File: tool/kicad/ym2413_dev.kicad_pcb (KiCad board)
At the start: 2 copper layers, 34 parts, among them P1 CONN_4, U1 YM2413, X1 CRYSTAL

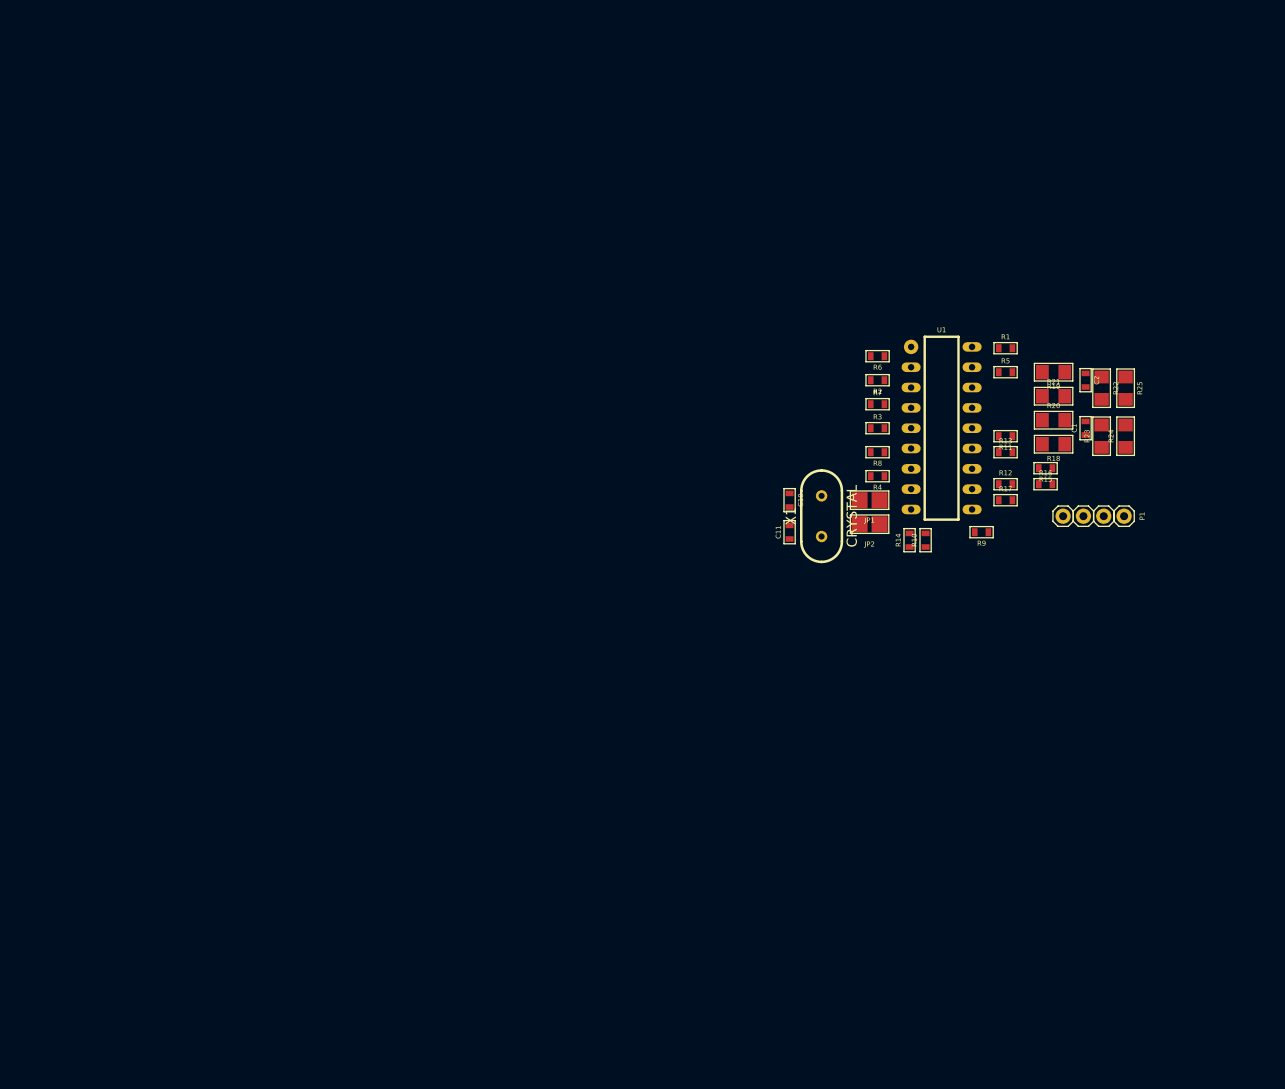
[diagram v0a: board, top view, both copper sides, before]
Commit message: cleanup; assign pins; add test points; restart pcb layout from zero
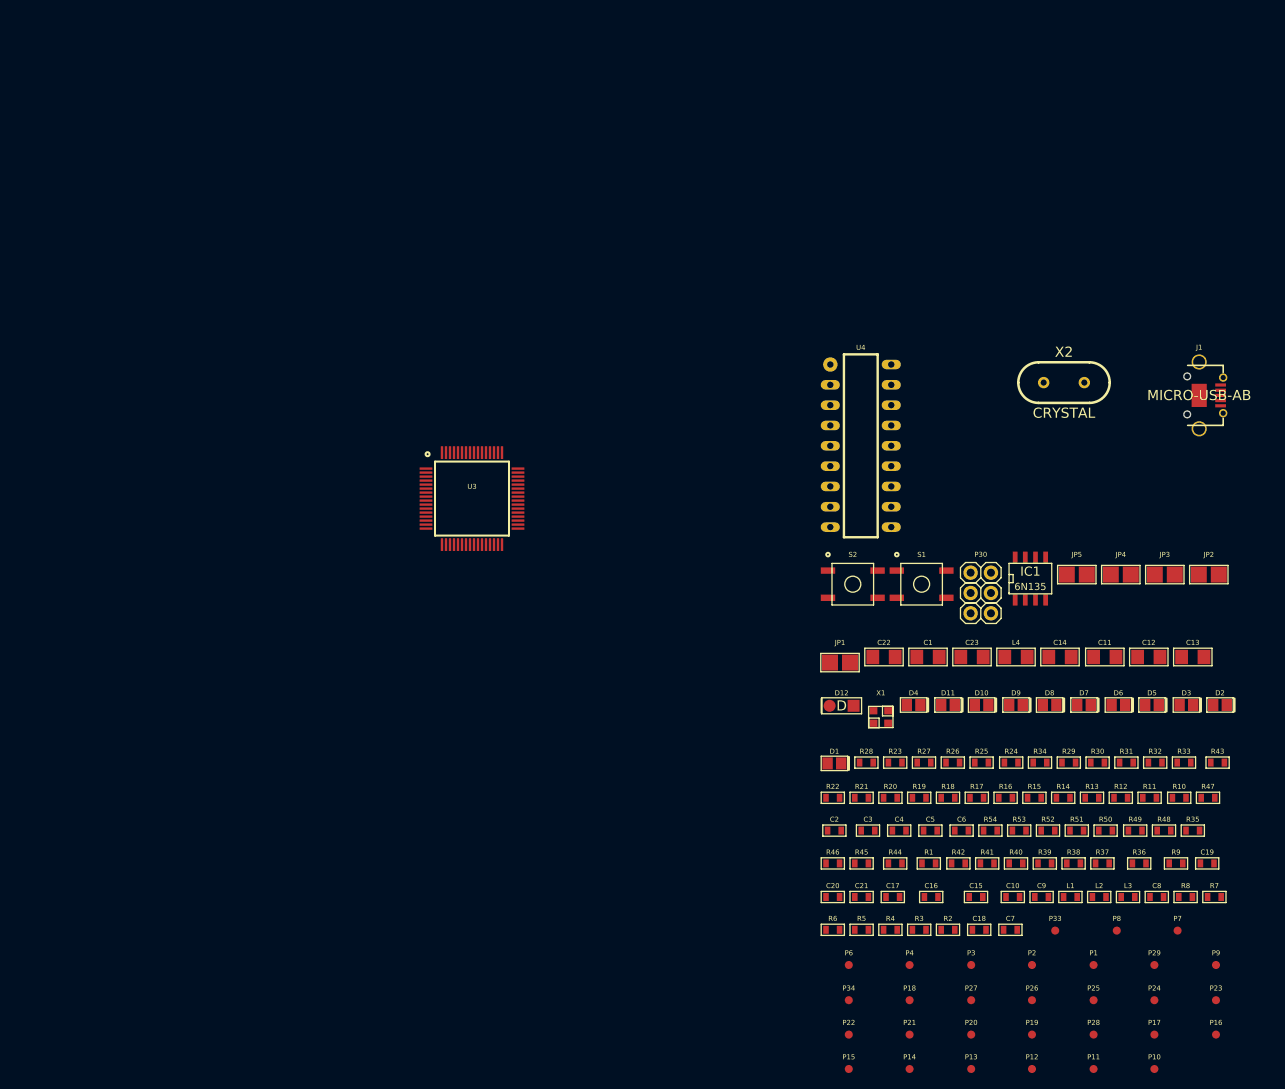
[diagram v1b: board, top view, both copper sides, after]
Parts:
- removed U1: YM2413, DIL18
- added C12: 4.7uF, 1206, F.Cu at (172.9, 126.6)
- added C13: 10uF, 1206, F.Cu at (178.4, 126.6)
- added C14: 10uF, 1206, F.Cu at (161.8, 126.6)
- added C15: 20pF/NC, 0603_S, F.Cu at (151.3, 156.6)
- added C16: 20pF/NC, 0603_S, F.Cu at (145.7, 156.6)
- added C17: 100nF, 0603_S, F.Cu at (140.9, 156.6)
- added C18: 2.2nF, 0603_S, F.Cu at (151.7, 160.7)
- added C19: 2.2nF, 0603_S, F.Cu at (180.2, 152.4)
- added C20: 1uF, 0603_S, F.Cu at (133.4, 156.6)
- added C21: 1uF, 0603_S, F.Cu at (137.0, 156.6)
- added C22: 10uF, 1206, F.Cu at (139.8, 126.6)
- added C23: 10uF, 1206, F.Cu at (150.8, 126.6)
- added C3: 100nF, 0603_S, F.Cu at (137.8, 148.3)
- added C4: 18pF, 0603_S, F.Cu at (141.7, 148.3)
- added C5: 100nF, 0603_S, F.Cu at (145.6, 148.3)
- added C6: 18pF, 0603_S, F.Cu at (149.5, 148.3)
- added C7: 1uF, 0603_S, F.Cu at (155.6, 160.7)
- added C8: 10nF, 0603_S, F.Cu at (173.9, 156.6)
- added C9: 1uF, 0603_S, F.Cu at (159.5, 156.6)
- added D1: LED, 0805_LED, F.Cu at (133.6, 139.9)
- added D10: LED, 0805_LED, F.Cu at (152.0, 132.6)
- added D11: LED, 0805_LED, F.Cu at (147.8, 132.6)
- added D12: D, TAIW_SEM_DIODE, F.Cu at (134.5, 132.7)
- added D2: LED, 0805_LED, F.Cu at (181.8, 132.6)
- added D3: LED, 0805_LED, F.Cu at (177.6, 132.6)
- added D4: LED, 0805_LED, F.Cu at (143.5, 132.6)
- added D5: LED, 0805_LED, F.Cu at (173.3, 132.6)
- added D6: LED, 0805_LED, F.Cu at (169.1, 132.6)
- added D7: LED, 0805_LED, F.Cu at (164.8, 132.6)
- added D8: LED, 0805_LED, F.Cu at (160.5, 132.6)
- added D9: LED, 0805_LED, F.Cu at (156.3, 132.6)
- added IC1: 6N135, SO8E, F.Cu at (158.1, 116.8)
- added J1: MICRO-USB-AB, USB-MICRO-AB-Molex-47590-0001, F.Cu at (179.2, 93.9)
- added JP3: SJ, Solder_Jumper_2mm, F.Cu at (174.9, 116.3)
- added JP4: SJ, Solder_Jumper_2mm, F.Cu at (169.4, 116.3)
- added JP5: SJ, Solder_Jumper_2mm, F.Cu at (163.9, 116.3)
- added L1: FB, 0603_S, F.Cu at (163.1, 156.6)
- added L2: FB, 0603_S, F.Cu at (166.7, 156.6)
- added L3: FB, 0603_S, F.Cu at (170.3, 156.6)
- added L4: L, 1206, F.Cu at (156.3, 126.6)
- added P10: TEST_POINT, Test_Pad_1mm, F.Cu at (173.6, 178.1)
- added P11: TEST_POINT, Test_Pad_1mm, F.Cu at (166.0, 178.1)
- added P12: TEST_POINT, Test_Pad_1mm, F.Cu at (158.3, 178.1)
- added P13: TEST_POINT, Test_Pad_1mm, F.Cu at (150.7, 178.1)
- added P14: TEST_POINT, Test_Pad_1mm, F.Cu at (143.0, 178.1)
- added P15: TEST_POINT, Test_Pad_1mm, F.Cu at (135.4, 178.1)
- added P16: TEST_POINT, Test_Pad_1mm, F.Cu at (181.3, 173.8)
- added P17: TEST_POINT, Test_Pad_1mm, F.Cu at (173.6, 173.8)
- added P18: TEST_POINT, Test_Pad_1mm, F.Cu at (143.0, 169.5)
- added P19: TEST_POINT, Test_Pad_1mm, F.Cu at (158.3, 173.8)
- added P2: TEST_POINT, Test_Pad_1mm, F.Cu at (158.3, 165.1)
- added P20: TEST_POINT, Test_Pad_1mm, F.Cu at (150.7, 173.8)
- added P21: TEST_POINT, Test_Pad_1mm, F.Cu at (143.0, 173.8)
- added P22: TEST_POINT, Test_Pad_1mm, F.Cu at (135.4, 173.8)
- added P23: TEST_POINT, Test_Pad_1mm, F.Cu at (181.3, 169.5)
- added P24: TEST_POINT, Test_Pad_1mm, F.Cu at (173.6, 169.5)
- added P25: TEST_POINT, Test_Pad_1mm, F.Cu at (166.0, 169.5)
- added P26: TEST_POINT, Test_Pad_1mm, F.Cu at (158.3, 169.5)
- added P27: TEST_POINT, Test_Pad_1mm, F.Cu at (150.7, 169.5)
- added P28: TEST_POINT, Test_Pad_1mm, F.Cu at (166.0, 173.8)
- added P29: TEST_POINT, Test_Pad_1mm, F.Cu at (173.6, 165.1)
- added P3: TEST_POINT, Test_Pad_1mm, F.Cu at (150.7, 165.1)
- added P30: CONN_3X2, PIN_2X3_ALT_S, F.Cu at (151.9, 118.6)
- added P33: TEST_POINT, Test_Pad_1mm, F.Cu at (161.2, 160.8)
- added P34: TEST_POINT, Test_Pad_1mm, F.Cu at (135.4, 169.5)
- added P4: TEST_POINT, Test_Pad_1mm, F.Cu at (143.0, 165.1)
- added P6: TEST_POINT, Test_Pad_1mm, F.Cu at (135.4, 165.1)
- added P7: TEST_POINT, Test_Pad_1mm, F.Cu at (176.5, 160.8)
- added P8: TEST_POINT, Test_Pad_1mm, F.Cu at (168.9, 160.8)
- added P9: TEST_POINT, Test_Pad_1mm, F.Cu at (181.3, 165.1)
- added R26: 22, 0603_S, F.Cu at (148.4, 139.8)
- added R27: 22, 0603_S, F.Cu at (144.8, 139.8)
- added R28: 22, 0603_S, F.Cu at (137.6, 139.8)
- added R29: 22, 0603_S, F.Cu at (162.9, 139.8)
- added R30: 22, 0603_S, F.Cu at (166.5, 139.8)
- added R31: 100k, 0603_S, F.Cu at (170.1, 139.8)
- added R32: 22, 0603_S, F.Cu at (173.7, 139.8)
- added R33: 22, 0603_S, F.Cu at (177.3, 139.8)
- added R34: 22, 0603_S, F.Cu at (159.3, 139.8)
- added R35: 100k, 0603_S, F.Cu at (178.4, 148.3)
- added R36: 100k/NC, 0603_S, F.Cu at (171.7, 152.4)
- added R37: 10k, 0603_S, F.Cu at (167.1, 152.4)
- added R38: 100, 0603_S, F.Cu at (163.5, 152.4)
- added R39: 10k, 0603_S, F.Cu at (159.9, 152.4)
- added R40: 2k2, 0603_S, F.Cu at (156.3, 152.4)
- added R41: 2k2, 0603_S, F.Cu at (152.7, 152.4)
- added R42: 100, 0603_S, F.Cu at (149.1, 152.4)
- added R43: 4k7/NC, 0603_S, F.Cu at (181.5, 139.8)
- added R44: 4k7/NC, 0603_S, F.Cu at (141.2, 152.4)
- added R45: 2k2, 0603_S, F.Cu at (137.0, 152.4)
- added R46: 2k2, 0603_S, F.Cu at (133.4, 152.4)
- added R47: 2k2, 0603_S, F.Cu at (180.3, 144.2)
- added R48: 100, 0603_S, F.Cu at (174.8, 148.3)
- added R49: 100, 0603_S, F.Cu at (171.2, 148.3)
- added R50: 2k2, 0603_S, F.Cu at (167.5, 148.3)
- added R51: 2k2, 0603_S, F.Cu at (163.9, 148.3)
- added R52: 2k2, 0603_S, F.Cu at (160.3, 148.3)
- added R53: 1k, 0603_S, F.Cu at (156.7, 148.3)
- added R54: 1k, 0603_S, F.Cu at (153.1, 148.3)
- added S1: TACTSW, BUTTON_ALPS_SMD_5.2mm_SKQG_S, F.Cu at (144.5, 117.5)
- added S2: TACTSW, BUTTON_ALPS_SMD_5.2mm_SKQG_S, F.Cu at (135.9, 117.5)
- added U3: EFM32GG332, TQFP64, F.Cu at (88.3, 106.8)
- added U4: YM2413, DIL18, F.Cu at (136.9, 100.2)
- added X2: CRYSTAL, HC-49V, F.Cu at (162.3, 92.3)
- C1: value ? -> 10uF; footprint 0603_S -> 1206
- C10: value 20pF/NC -> 10nF
- C11: value 20pF/NC -> 10uF; footprint 0603_S -> 1206
- C2: value ? -> 100nF
- P1: value CONN_4 -> TEST_POINT; footprint PIN_1X4_S -> Test_Pad_1mm
- R1, R10, R2, R3, R4, R5, R6, R7, R8, R9: value 22 -> 3k3
- R11: value 22 -> 1
- R12, R14: value 22 -> 15
- R13: value 100k -> 3k3
- R15: value 22 -> 220
- R16: value 100k -> 220
- R17: value 100k/NC -> 22
- R18, R19, R22, R23, R24, R25: value 2k2 -> 22; footprint 1206 -> 0603_S
- R20, R21: value 4k7/NC -> 22; footprint 1206 -> 0603_S
- X1: value CRYSTAL -> 48Mhz; footprint HC-49V -> CRYSTAL-TXC-8Z-2.5x2
- moved R7 74.6 mm to (181.1, 156.6)
- moved R5 72.0 mm to (137.0, 160.7)
- moved R6 71.9 mm to (133.4, 160.7), turned to 0 degrees
- moved R2 69.3 mm to (147.8, 160.7), turned to 0 degrees
- moved R8 67.6 mm to (177.5, 156.6), turned to 0 degrees
- moved R1 65.1 mm to (145.4, 152.4)
- moved C2 64.5 mm to (133.6, 148.3), turned to 0 degrees
- moved R3 62.9 mm to (144.2, 160.7)
- moved R22 61.2 mm to (133.4, 144.2), turned to 0 degrees
- moved C10 56.9 mm to (155.9, 156.6), turned to 0 degrees
- moved R4 56.7 mm to (140.6, 160.7), turned to 0 degrees
- moved P1 56.1 mm to (166.0, 165.1), turned to 0 degrees
- moved R19 55.8 mm to (144.2, 144.2), turned to 0 degrees
- moved R21 55.6 mm to (137.0, 144.2)
- moved R20 51.4 mm to (140.6, 144.2)
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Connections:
- net /XOUT renamed /D+B
- C1 pad 2: N-000001 -> +3.3V
- C10 pad 1: N-0000033 -> GND
- C10 pad 2: GND -> N-0000029
- C11 pad 1: N-000003 -> GND
- C11 pad 2: GND -> N-0000029
- C2 pad 2: N-0000014 -> +3.3V
- JP1 pad 1: /XIN' -> GND
- JP1 pad 2: N-0000033 -> /XOUT'
- JP2 pad 1: /XOUT' -> /XIN'
- JP2 pad 2: N-000003 -> N-0000018
- P1 pad 1: /RO/2 -> /XIN
- R1 pad 1: /D1' -> N-0000089
- R1 pad 2: /D1 -> +5V
- R10 pad 1: /XIN -> N-0000037
- R10 pad 2: /XIN' -> /LED8
- R11 pad 1: /~IC -> N-0000028
- R11 pad 2: /~IC' -> N-0000029
- R12 pad 1: /~WE -> /D-B
- R12 pad 2: /~WE' -> /D-
- R13 pad 1: /~IC' -> N-0000036
- R13 pad 2: +5V -> /LED9
- R14 pad 2: /XOUT' -> /D+
- R15 pad 1: /~CS -> N-0000020
- R15 pad 2: /~CS' -> N-000005
- R16 pad 1: /~CS' -> +3.3V
- R16 pad 2: +5V -> /MIDI_IN
- R17 pad 1: /~WE' -> /D1'
- R17 pad 2: +5V -> /D1
- R18 pad 1: GND -> /D3'
- R18 pad 2: /MO -> /D3
- R19 pad 1: GND -> /D5'
- R19 pad 2: /RO -> /D5
- R2 pad 1: /D3' -> N-0000091
- R2 pad 2: /D3 -> /LED0
- R20 pad 1: /MO -> /D7'
- R20 pad 2: N-000001 -> /D7
- R21 pad 1: /RO -> /D0'
- R21 pad 2: N-0000014 -> /D0
- R22 pad 1: /RO/2 -> /D2'
- R22 pad 2: N-0000014 -> /D2
- R23 pad 1: /MO/2 -> /D4'
- R23 pad 2: N-000001 -> /D4
- R24 pad 1: /MO/2 -> /D6'
- R24 pad 2: GND -> /D6
- R25 pad 1: /RO/2 -> /~WE'
- R25 pad 2: GND -> /~WE
- R3 pad 1: /D5' -> N-0000083
- R3 pad 2: /D5 -> /LED1
- R4 pad 1: /D7' -> N-0000085
- R4 pad 2: /D7 -> /LED2
- R5 pad 1: /D0' -> N-0000086
- R5 pad 2: /D0 -> /LED3
- R6 pad 1: /D2' -> N-0000087
- R6 pad 2: /D2 -> /LED4
- R7 pad 1: /D4' -> N-0000046
- R7 pad 2: /D4 -> /LED5
- R8 pad 1: /D6' -> N-0000048
- R8 pad 2: /D6 -> /LED6
- R9 pad 1: /A0 -> N-0000051
- R9 pad 2: /A0' -> /LED7
- X1 pad 1: N-000003 -> N-0000032
- X1 pad 2: N-0000033 -> GND
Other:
- board outline added: 0.8 x 5.6 mm

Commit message: add 6-pin FTDI debug header
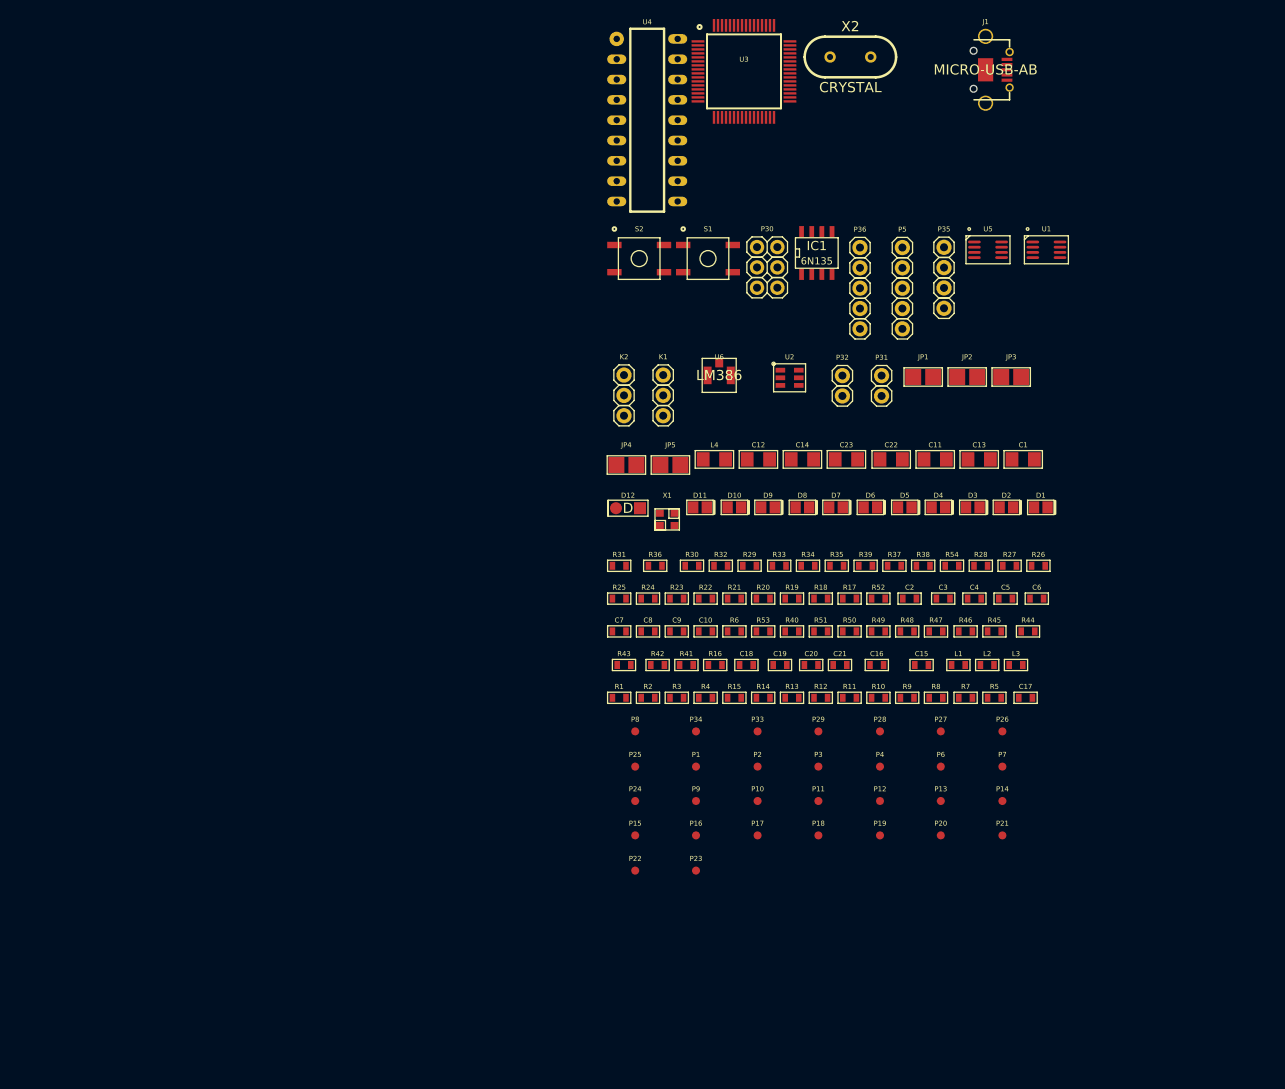
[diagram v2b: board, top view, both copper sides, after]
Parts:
- added K1: CONN_3, PIN_1X3, F.Cu at (112.2, 93.9)
- added K2: CONN_3, PIN_1X3, F.Cu at (107.3, 93.9)
- added P31: CONN_2, PIN_1X2_S, F.Cu at (139.5, 92.7)
- added P32: CONN_2, PIN_1X2_S, F.Cu at (134.6, 92.7)
- added P35: CONN_6, PIN_1X4_S, F.Cu at (147.3, 79.2)
- added P36: CONN_5, PIN_1X5_S, F.Cu at (136.8, 80.5)
- added P5: MIDI-IN, PIN_1X5_S, F.Cu at (142.1, 80.5)
- added U1: SN74LVC2T45, R-PDSO-G8, F.Cu at (160.1, 75.7)
- added U2: ST-USBLC6-2, SOT-23-6L, F.Cu at (128.0, 91.7)
- added U5: LM386, R-PDSO-G8, F.Cu at (152.8, 75.7)
- added U6: LM386, HRS-U.FL-R-SMT, F.Cu at (119.2, 91.4)
- moved R43 75.2 mm to (107.3, 127.6)
- moved C8 71.7 mm to (110.3, 123.4)
- moved R36 71.0 mm to (111.2, 115.2)
- moved P16 69.6 mm to (116.3, 148.9)
- moved P24 69.5 mm to (108.7, 144.6)
- moved P9 68.2 mm to (116.3, 144.6)
- moved R31 68.0 mm to (106.7, 115.2)
- moved P23 67.0 mm to (116.3, 153.3)
- moved P8 65.1 mm to (108.7, 135.9)
- moved P25 64.3 mm to (108.7, 140.3)
- moved U3 63.3 mm to (122.3, 53.4)
- moved JP4 63.3 mm to (107.6, 102.6)
- moved C7 61.5 mm to (106.7, 123.4)
- moved P10 59.9 mm to (124.0, 144.6)
- moved R32 59.6 mm to (119.4, 115.2)
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
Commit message: rough layout
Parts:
- removed R29, R30, R33: 22, 0603_S
- added P37: TEST_POINT, Test_Pad_1mm, F.Cu at (144.0, 84.5)
- added P38: TEST_POINT, Test_Pad_1mm, F.Cu at (144.0, 87.0)
- IC1: footprint SO8E -> DIL8
- P35: footprint PIN_1X4_S -> PIN_1X6_S
- U6: footprint HRS-U.FL-R-SMT -> R-PDSO-G8
- moved C17 130.4 mm to (44.0, 67.5)
- moved J1 116.9 mm to (40.0, 85.0)
- moved L3 116.1 mm to (49.5, 82.0), turned to 180 degrees
- moved L2 116.0 mm to (46.0, 82.0), turned to 180 degrees
- moved P35 114.3 mm to (34.5, 61.0)
- moved R38 112.7 mm to (44.0, 64.5)
- moved L1 110.4 mm to (46.0, 88.0), turned to 180 degrees
- moved D1 105.3 mm to (54.5, 116.5), turned to 270 degrees
- moved P7 101.1 mm to (81.5, 70.5)
- moved D2 96.5 mm to (59.0, 116.5), turned to 270 degrees
- moved P6 96.0 mm to (80.0, 71.5)
- moved P13 95.0 mm to (87.5, 70.5)
- moved R12 93.9 mm to (51.0, 84.0)
- moved R42 90.6 mm to (53.5, 58.0), turned to 270 degrees
- moved D3 89.3 mm to (62.0, 116.5), turned to 270 degrees
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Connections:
- net N-0000013 renamed /MOA2
- net N-0000014 renamed /MOI2
- net N-0000021 renamed /ROA3
- net N-0000031 renamed /ROI2
- net N-0000034 renamed /ROA
- C10 pad 2: N-0000039 (its old number) -> +3.3VADC
- C11 pad 2: N-0000039 (its old number) -> +3.3VADC
- C21 pad 2: N-000009 (its old number) -> /MOA
- C22 pad 2: N-0000010 (its old number) -> /ROA2
- C23 pad 1: N-000009 (its old number) -> /MOA
- C8 pad 2: N-0000039 (its old number) -> +3.3VADC
- K2 pad 2: N-0000012 (its old number) -> /MOA3
- P1 pad 1: /XIN -> /XOUT
- P2 pad 1: /XOUT -> /XIN
- P35 pad 1: N-0000061 (its old number) -> N-0000068
- R11 pad 2: N-0000039 (its old number) -> +3.3VADC
- R12 pad 1: /D-B -> /D+B
- R12 pad 2: /D- -> /D+
- R14 pad 1: /D+B -> /D-B
- R14 pad 2: /D+ -> /D-
- R48 pad 2: N-0000010 (its old number) -> /ROA2
- R51 pad 2: N-0000010 (its old number) -> /ROA2
- R52 pad 1: N-0000012 (its old number) -> /MOA3
- R54 pad 1: N-0000012 (its old number) -> /MOA3
- U1 pad 2: /XIN3V3 -> /XOUT3V3
- U1 pad 3: /XOUT3V3 -> /XIN3V3
- U1 pad 4: N-0000025 -> GND
- U1 pad 6: /XOUT -> /XIN
- U1 pad 7: /XIN -> /XOUT
- U2 pad 1: /D-_IN -> /D-B
- U2 pad 3: /D+_IN -> /D+B
- U2 pad 4: /D+B -> /D+_IN
- U2 pad 6: /D-B -> /D-_IN
- U3 pad 23: N-0000039 (its old number) -> +3.3VADC
- U3 pad 27: N-0000039 (its old number) -> +3.3VADC
- U3 pad 47: /D- -> /D+
- U3 pad 48: /D+ -> /D-
